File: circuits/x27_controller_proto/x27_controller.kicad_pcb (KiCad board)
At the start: 2 copper layers, 50 x 50 mm, 19 parts, among them J1 INPUT, J2 5V, M1 x27_Stepper, U1 74HC595

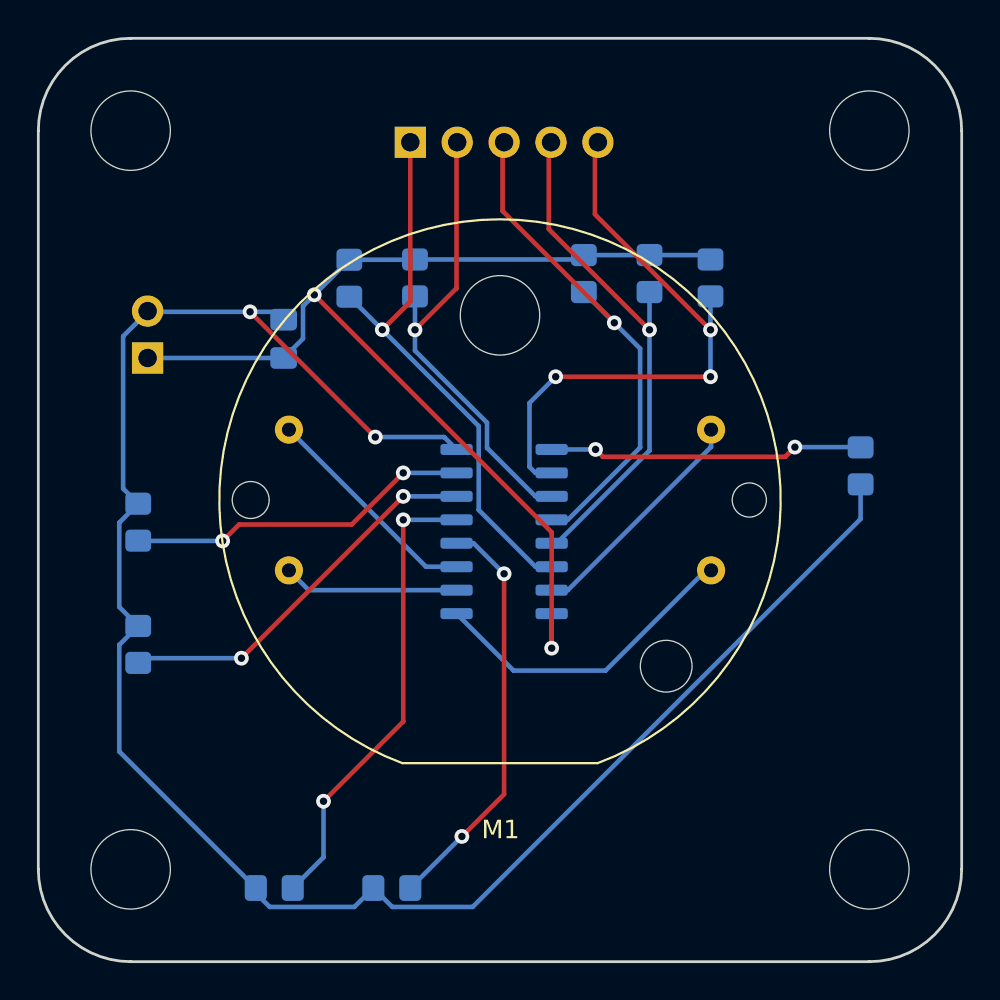
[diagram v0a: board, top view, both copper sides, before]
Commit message: Code works and is tested on waveforms.
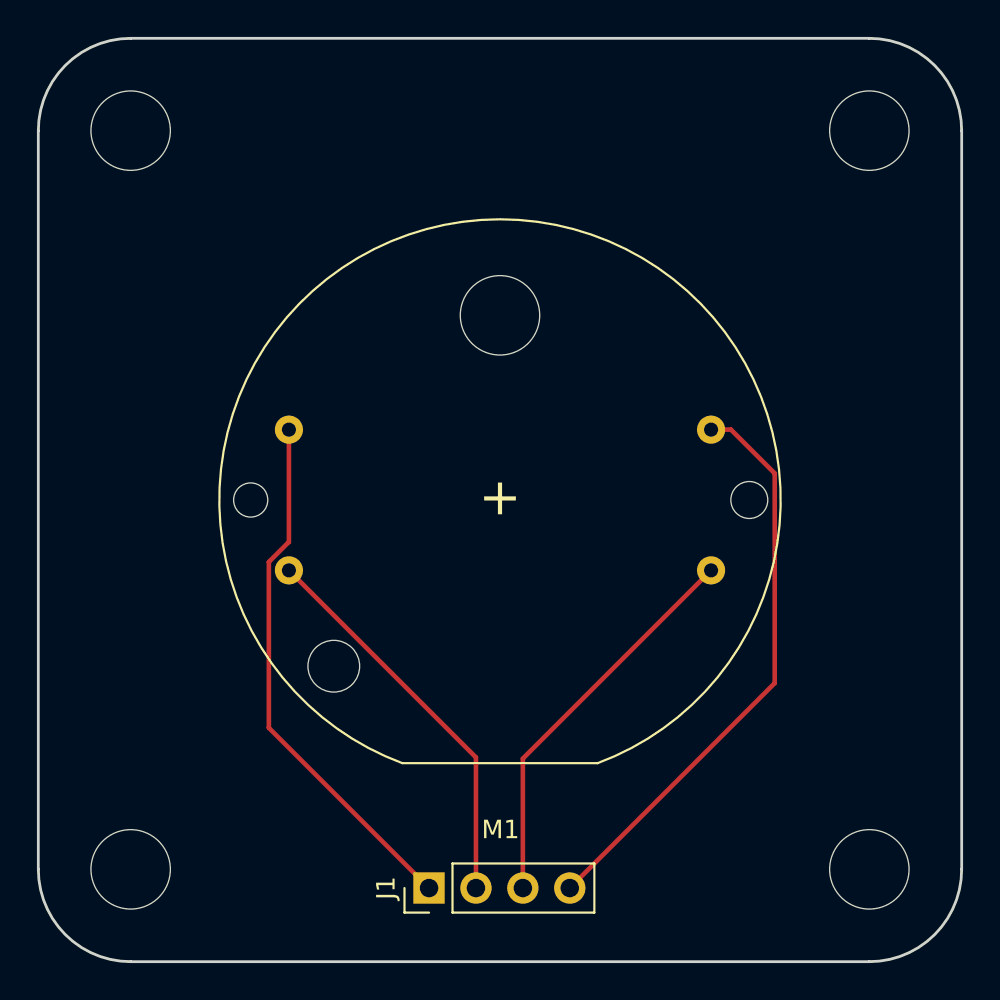
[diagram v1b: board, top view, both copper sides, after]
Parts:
- removed C1: 10 nF, Capacitor_SMD:C_0805_2012Metric_Pad1.18x1.45mm_HandSolder
- removed J2: 5V, Connector_PinHeader_2.54mm:PinHeader_1x02_P2.54mm_Vertical
- removed R1, R2, R3, R4, R5: 10K, Resistor_SMD:R_0805_2012Metric_Pad1.20x1.40mm_HandSolder
- removed R10, R6, R7, R8, R9: 1K, Resistor_SMD:R_0805_2012Metric_Pad1.20x1.40mm_HandSolder
- removed U1: 74HC595, Package_SO:SO-16_3.9x9.9mm_P1.27mm
- J1: value INPUT -> Conn_01x04; footprint Connector_PinHeader_2.54mm:PinHeader_1x05_P2.54mm_Vertical -> Connector_PinHeader_2.54mm:PinHeader_1x04_P2.54mm_Vertical; moved to F.Cu
- moved J1 40.4 mm to (121.2, 96.0), turned to 90 degrees
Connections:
- J1 pad 1: Net-(J1-Pad1) -> Net-(M1-Pad1)
- J1 pad 2: Net-(J1-Pad2) -> Net-(M1-Pad2)
- J1 pad 3: Net-(J1-Pad3) -> Net-(M1-Pad3)
- J1 pad 4: Net-(J1-Pad4) -> Net-(M1-Pad4)
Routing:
- net Earth: track 103.0 -> 0.00 mm, vias 2 -> 0
- net +5V: track 60.2 -> 0.00 mm, vias 2 -> 0
- net Net-(J1-Pad5): track 32.3 -> 0.00 mm, vias 3 -> 0
- net Net-(J1-Pad1): track 30.5 -> 0.00 mm, vias 1 -> 0
- net Net-(J1-Pad4): track 28.4 -> 0.00 mm, vias 1 -> 0
- net Net-(J1-Pad3): track 28.4 -> 0.00 mm, vias 1 -> 0
- net Net-(J1-Pad2): track 25.5 -> 0.00 mm, vias 1 -> 0
- net Net-(R9-Pad1): track 25.5 -> 0.00 mm, vias 2 -> 0
- net Net-(R10-Pad1): track 22.4 -> 0.00 mm, vias 2 -> 0
- net Net-(R8-Pad1): track 21.0 -> 0.00 mm, vias 2 -> 0
- net Net-(M1-Pad4): track 12.2 -> 31.5 mm
- net Net-(R7-Pad1): track 18.8 -> 0.00 mm, vias 2 -> 0
- net Net-(R6-Pad1): track 17.1 -> 0.00 mm, vias 2 -> 0
- net Net-(M1-Pad1): track 12.8 -> 28.9 mm
- net Net-(M1-Pad3): track 9.52 -> 21.4 mm
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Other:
- board text removed: "+"
- board text removed: "-"
- board text removed: "1"
- board text removed: "Connor Briggs PilotWave x27 Module"

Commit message: Added more pullups
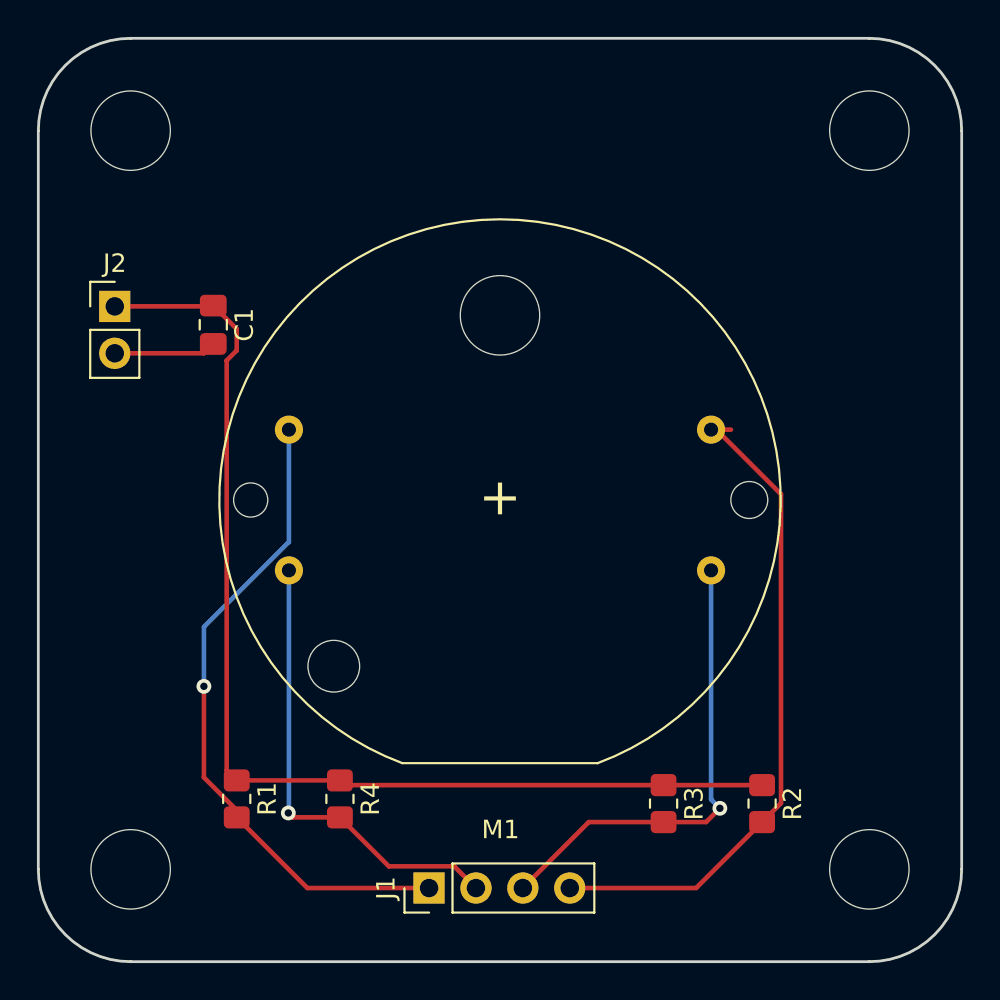
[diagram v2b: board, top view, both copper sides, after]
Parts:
- added C1: 10 nF, Capacitor_SMD:C_0805_2012Metric_Pad1.18x1.45mm_HandSolder, F.Cu at (109.5, 65.5)
- added J2: 5 V, Connector_PinHeader_2.54mm:PinHeader_1x02_P2.54mm_Vertical, F.Cu at (104.1, 64.5)
- added R1: 10 K, Resistor_SMD:R_0805_2012Metric_Pad1.20x1.40mm_HandSolder, F.Cu at (110.7, 91.2)
- added R2: 10 K, Resistor_SMD:R_0805_2012Metric_Pad1.20x1.40mm_HandSolder, F.Cu at (139.2, 91.4)
- added R3: 10 K, Resistor_SMD:R_0805_2012Metric_Pad1.20x1.40mm_HandSolder, F.Cu at (133.9, 91.4)
- added R4: 10 K, Resistor_SMD:R_0805_2012Metric_Pad1.20x1.40mm_HandSolder, F.Cu at (116.3, 91.2)
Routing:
- net +5V: track 0.00 -> 60.6 mm
- net Net-(J1-Pad1): track 28.9 -> 35.6 mm, vias 0 -> 1
- net Earth: track 0.00 -> 5.54 mm
- net Net-(J1-Pad4): track 31.5 -> 36.4 mm
- net Net-(J1-Pad3): track 21.4 -> 25.5 mm, vias 0 -> 1
- net Net-(J1-Pad2): track 21.4 -> 25.0 mm, vias 0 -> 1
